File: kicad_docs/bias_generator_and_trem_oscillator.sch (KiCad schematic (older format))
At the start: 31 parts, among them Q3 LND150, Q4 LND150

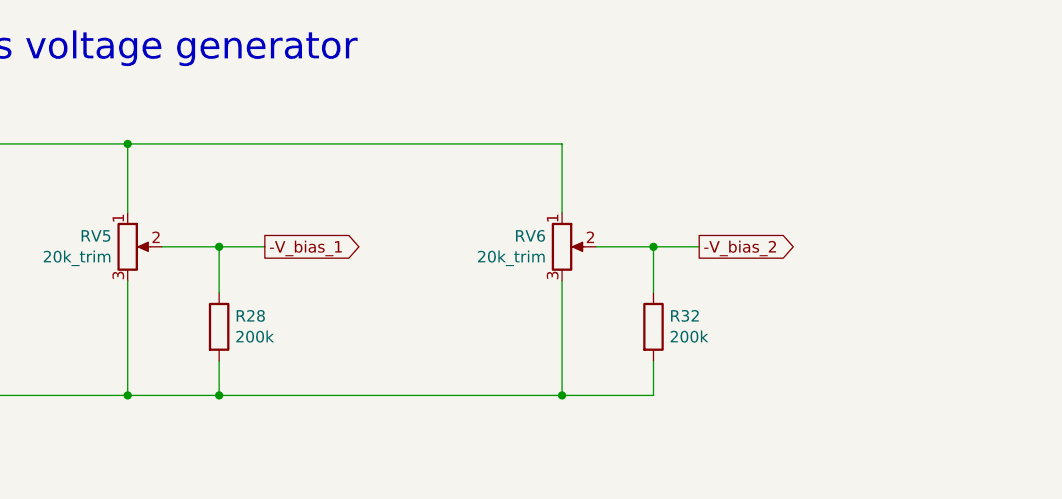
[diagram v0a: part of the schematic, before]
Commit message: add approximate voltages
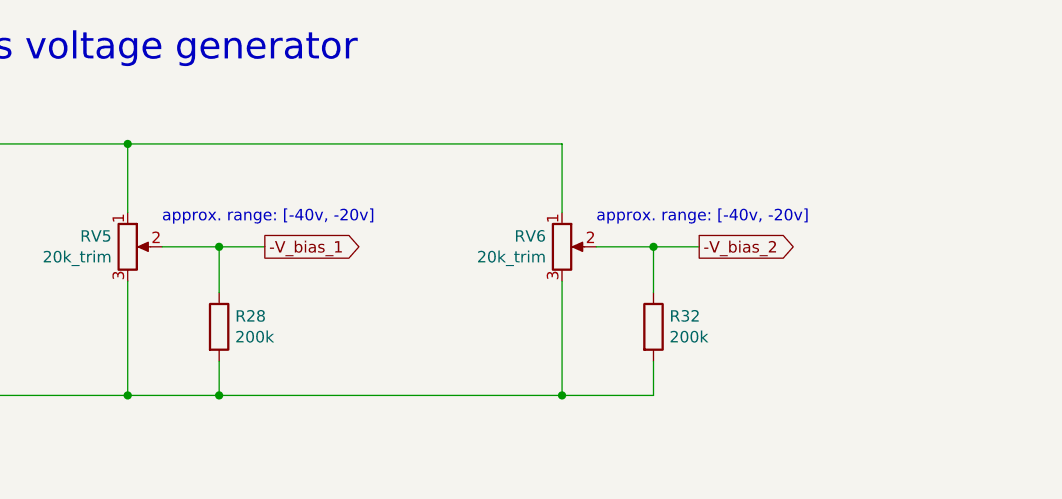
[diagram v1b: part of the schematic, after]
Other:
- note added: "approx. range: [-40v, -20v]"
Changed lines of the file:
@@
 Text Notes 4650 3250 0    118  ~ 0
 Tremolo oscillator
+Text Notes 5550 1600 0    50   ~ 0
+approx. range: [-40v, -20v]
+Text Notes 7450 1600 0    50   ~ 0
+approx. range: [-40v, -20v]
 $EndSCHEMATC
